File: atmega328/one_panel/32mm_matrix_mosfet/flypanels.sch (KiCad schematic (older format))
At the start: 16 parts, among them IC1 ATMEGA328-A, P1 CONN_8, P2 CONN_8, X1 CER_RESO

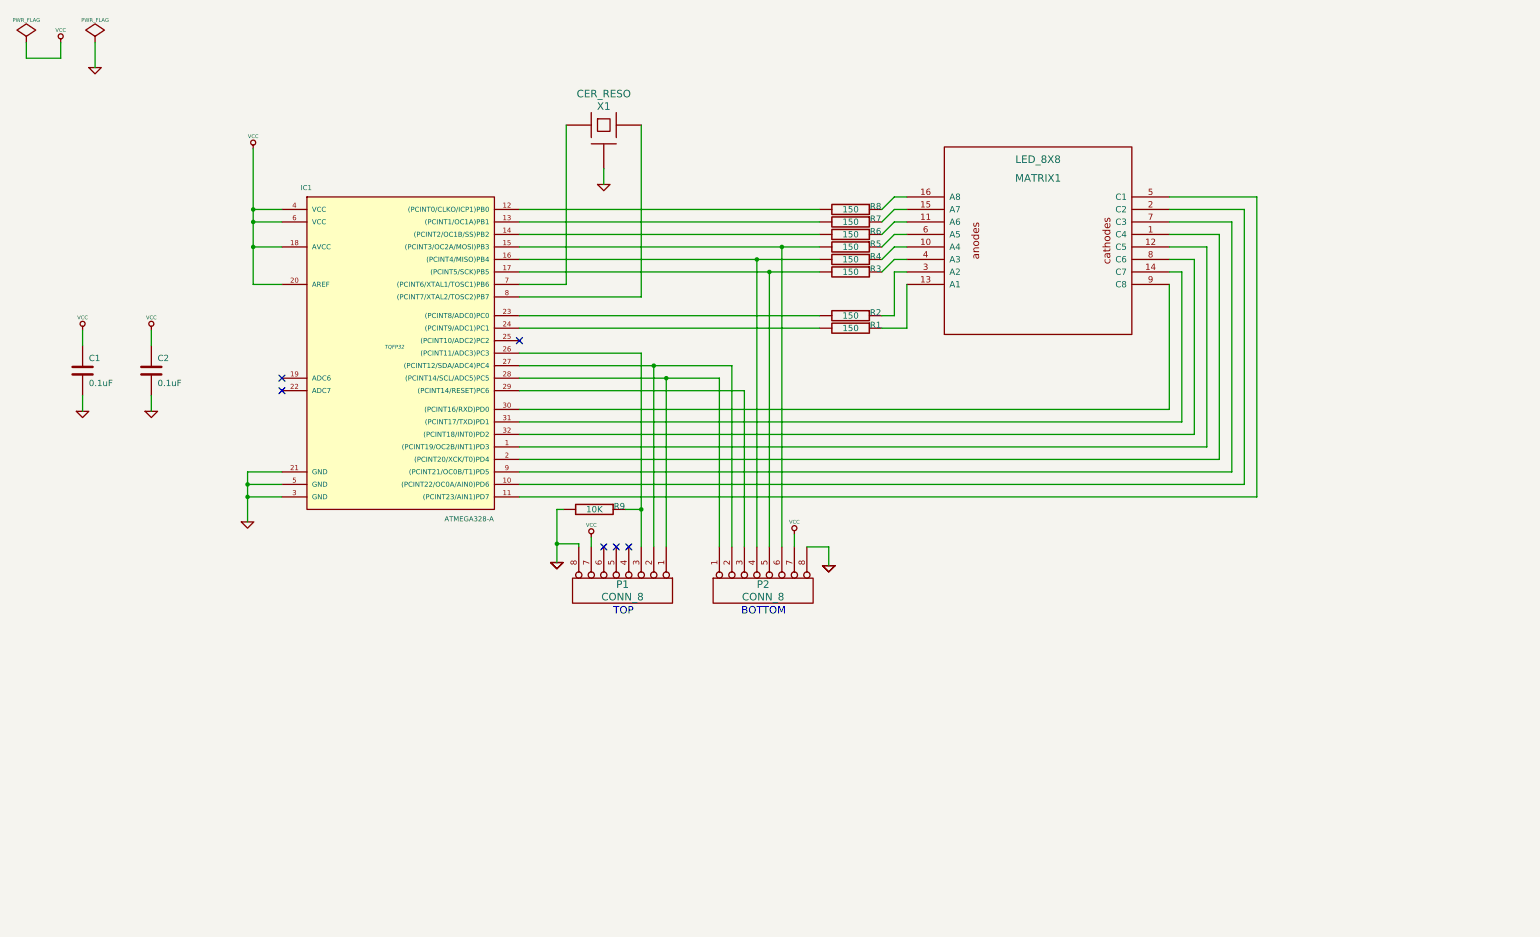
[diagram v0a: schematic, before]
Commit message: Added version of single matrix atmega328 design with mosfets.
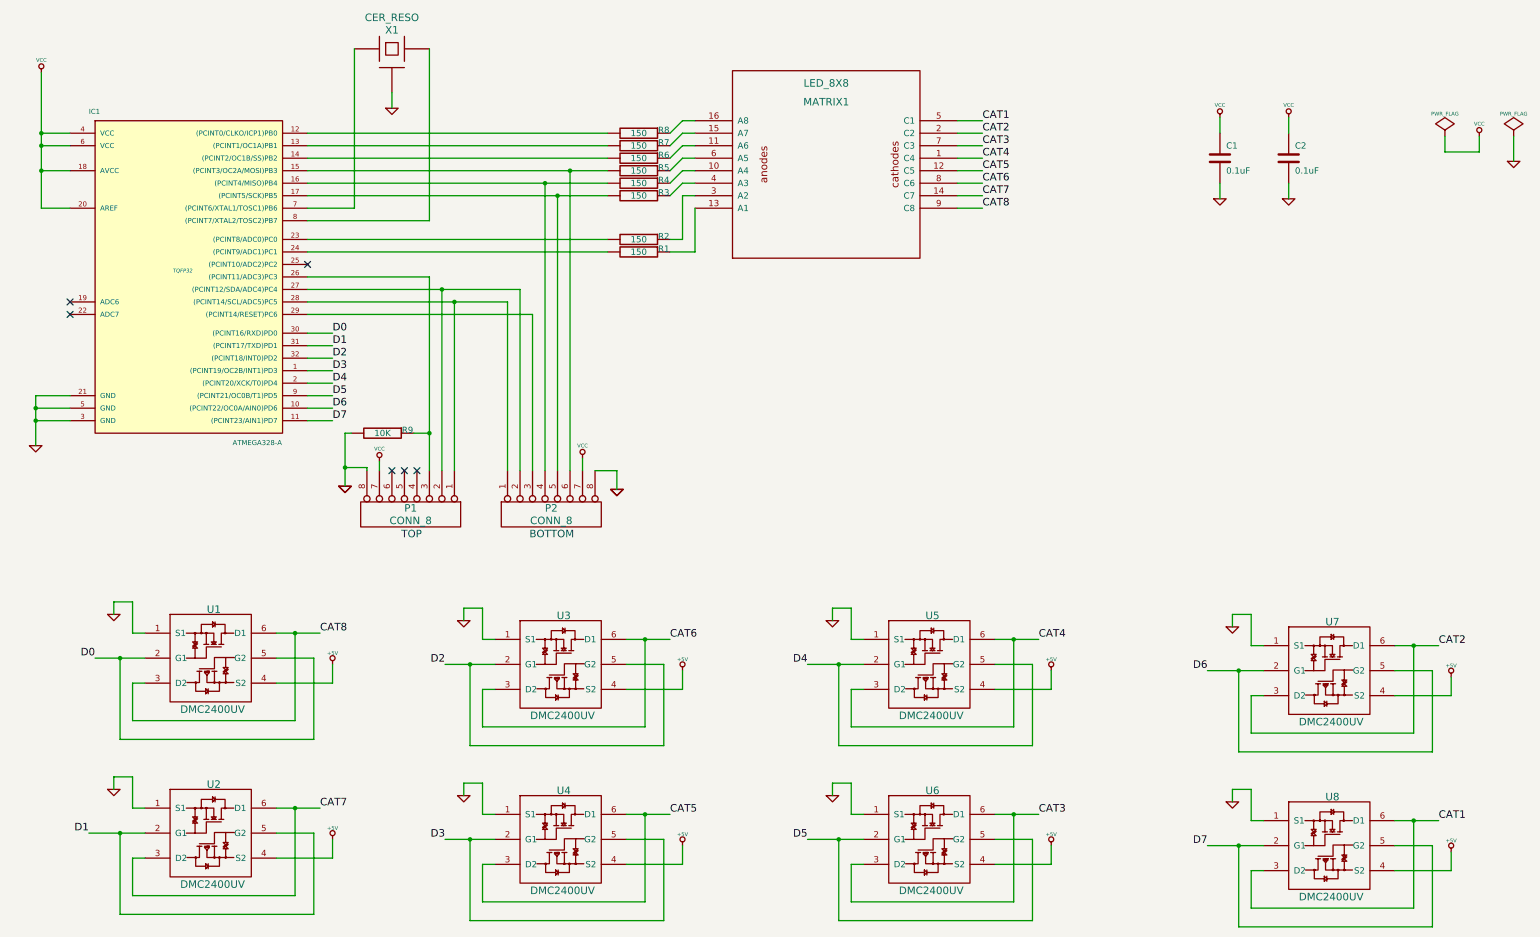
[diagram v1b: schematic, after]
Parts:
- added U1, U2, U3, U4, U5, U6, U7, U8: DMC2400UV, ~, symbol DMC2400UV
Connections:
- net GND: now also U1.1 (S1), U2.1 (S1), U3.1 (S1), U4.1 (S1), U5.1 (S1), U6.1 (S1), U7.1 (S1), U8.1 (S1)
- net CAT4: now reaches MATRIX1.1 (C4)
- net CAT4: now also U5.3 (D2), U5.6 (D1); no longer IC1.2 ((PCINT20/XCK/T0)PD4)
- net CAT5: now reaches MATRIX1.12 (C5)
- net CAT5: now also U4.3 (D2), U4.6 (D1); no longer IC1.1 ((PCINT19/OC2B/INT1)PD3)
- net CAT7: now reaches MATRIX1.14 (C7)
- net CAT7: now also U2.3 (D2), U2.6 (D1); no longer IC1.31 ((PCINT17/TXD)PD1)
- net CAT2: now reaches MATRIX1.2 (C2)
- net CAT2: now also U7.3 (D2), U7.6 (D1); no longer IC1.10 ((PCINT22/OC0A/AIN0)PD6)
- net CAT1: now reaches MATRIX1.5 (C1)
- net CAT1: now also U8.3 (D2), U8.6 (D1); no longer IC1.11 ((PCINT23/AIN1)PD7)
- net CAT3: now reaches MATRIX1.7 (C3)
- net CAT3: now also U6.3 (D2), U6.6 (D1); no longer IC1.9 ((PCINT21/OC0B/T1)PD5)
- net CAT6: now reaches MATRIX1.8 (C6)
- net CAT6: now also U3.3 (D2), U3.6 (D1); no longer IC1.32 ((PCINT18/INT0)PD2)
- net CAT8: now reaches MATRIX1.9 (C8)
- net CAT8: now also U1.3 (D2), U1.6 (D1); no longer IC1.30 ((PCINT16/RXD)PD0)
- new net +5V: U1.4 (S2), U2.4 (S2), U3.4 (S2), U4.4 (S2), U5.4 (S2), U6.4 (S2), U7.4 (S2), U8.4 (S2)
- new net D0: IC1.30 ((PCINT16/RXD)PD0), U1.2 (G1), U1.5 (G2)
- new net D1: IC1.31 ((PCINT17/TXD)PD1), U2.2 (G1), U2.5 (G2)
- new net D2: IC1.32 ((PCINT18/INT0)PD2), U3.2 (G1), U3.5 (G2)
- new net D3: IC1.1 ((PCINT19/OC2B/INT1)PD3), U4.2 (G1), U4.5 (G2)
- new net D4: IC1.2 ((PCINT20/XCK/T0)PD4), U5.2 (G1), U5.5 (G2)
- new net D5: IC1.9 ((PCINT21/OC0B/T1)PD5), U6.2 (G1), U6.5 (G2)
- new net D6: IC1.10 ((PCINT22/OC0A/AIN0)PD6), U7.2 (G1), U7.5 (G2)
- new net D7: IC1.11 ((PCINT23/AIN1)PD7), U8.2 (G1), U8.5 (G2)
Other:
- moved on the sheet: C1, C2, IC1, MATRIX1, P1, P2, R1, R2, R3, R4, R5, R6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

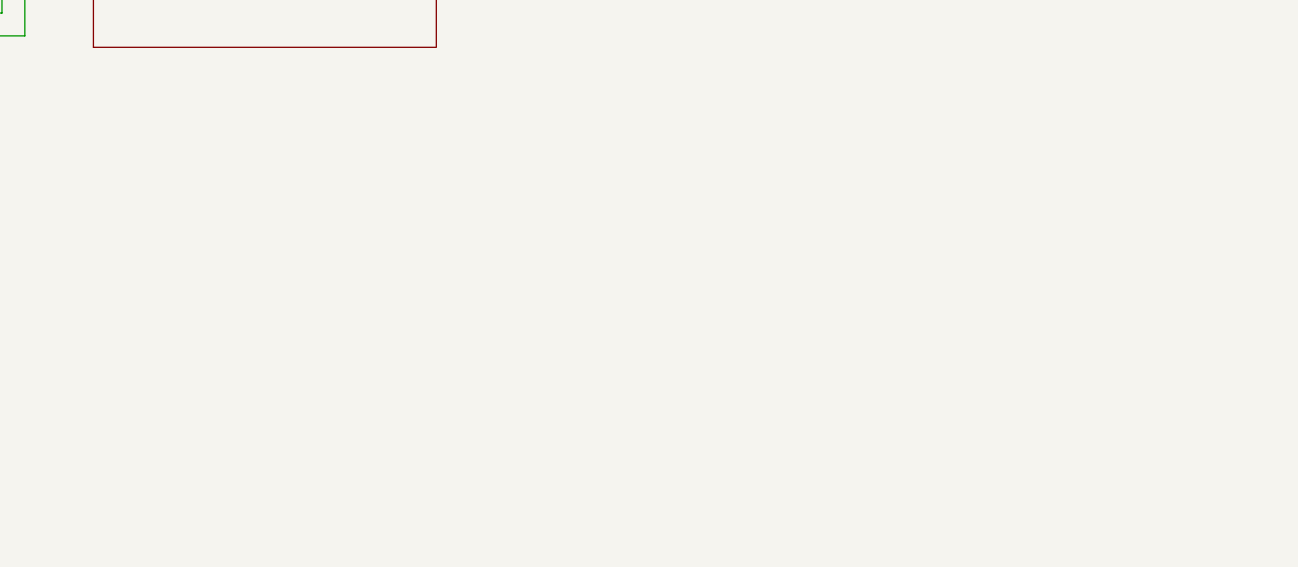
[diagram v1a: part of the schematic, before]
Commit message: Added note about error to atmega328 design.
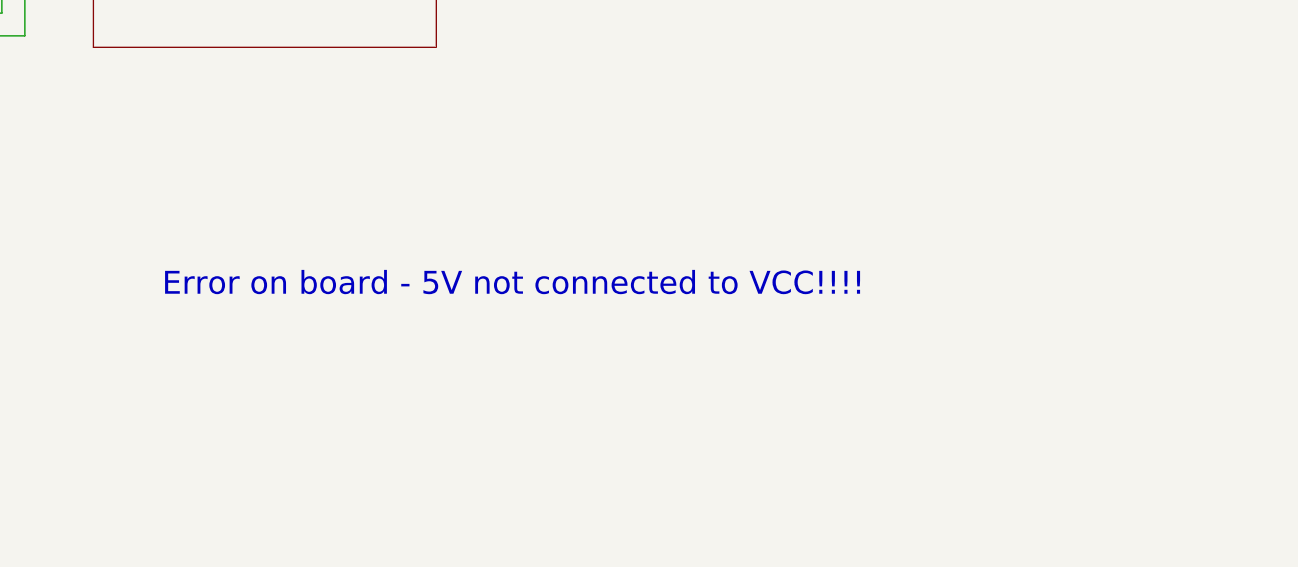
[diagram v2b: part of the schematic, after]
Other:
- note added: "Error on board - 5V not connected to VCC!!!!"
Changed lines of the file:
@@
 Sheet 1 1
 Title ""
-Date "22 may 2016"
+Date "24 jul 2016"
 Rev ""
 Comp ""
@@
 Text Label 3250 5650 0    60   ~ 0
 CAT8
+Text Notes 6850 3750 0    100  ~ 0
+Error on board - 5V not connected to VCC!!!!
 $EndSCHEMATC

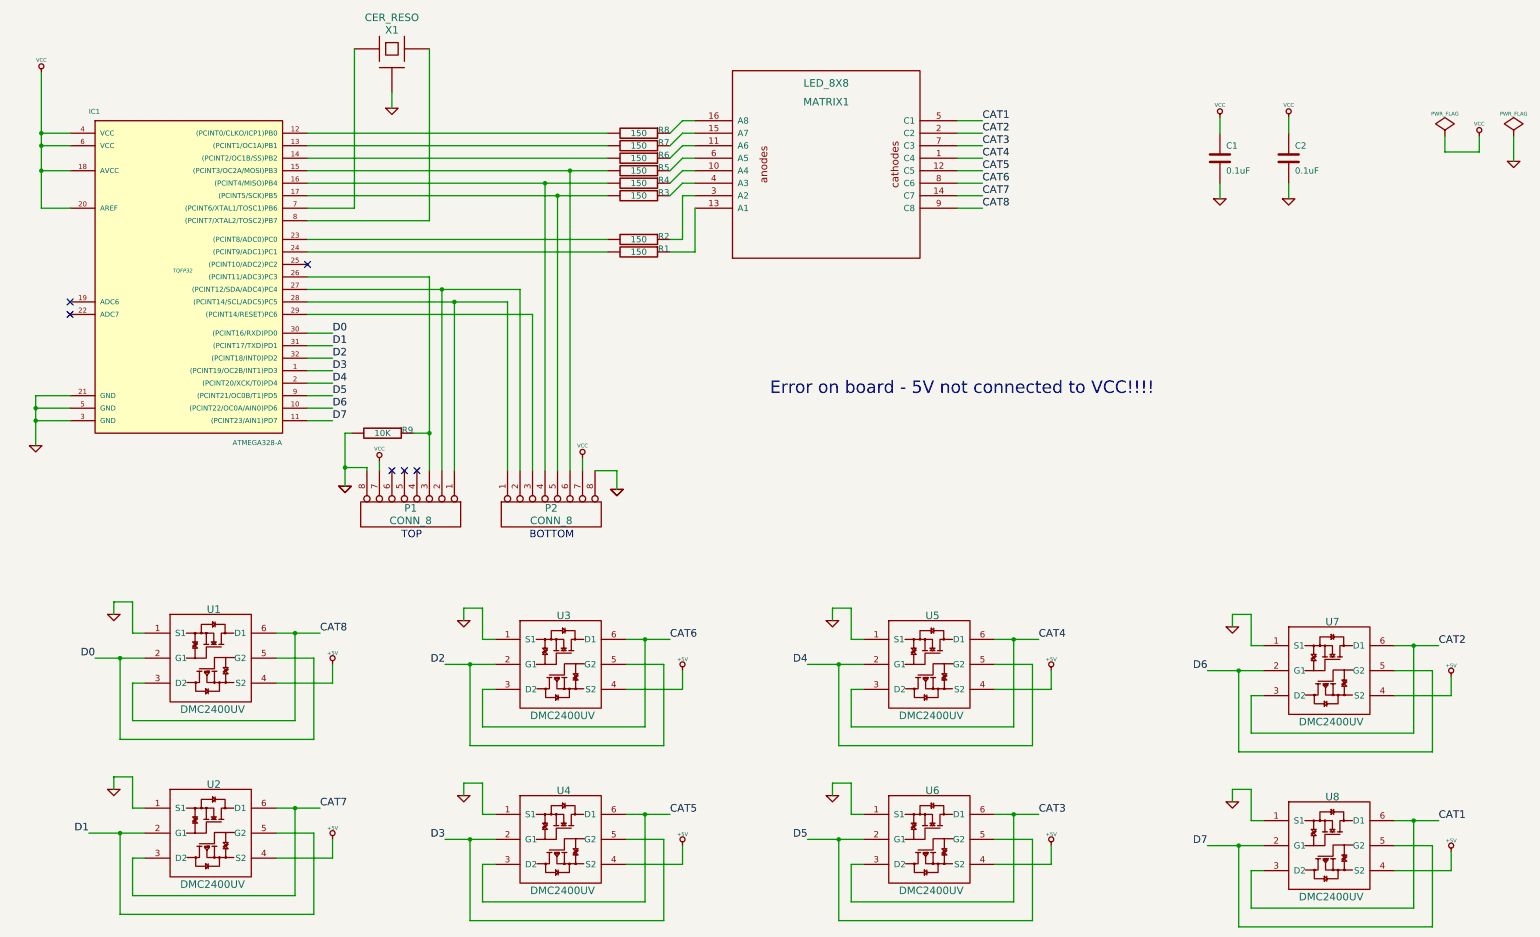
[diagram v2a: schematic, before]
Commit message: Added gerber files for 2nd revision of one matrix atmeg328.
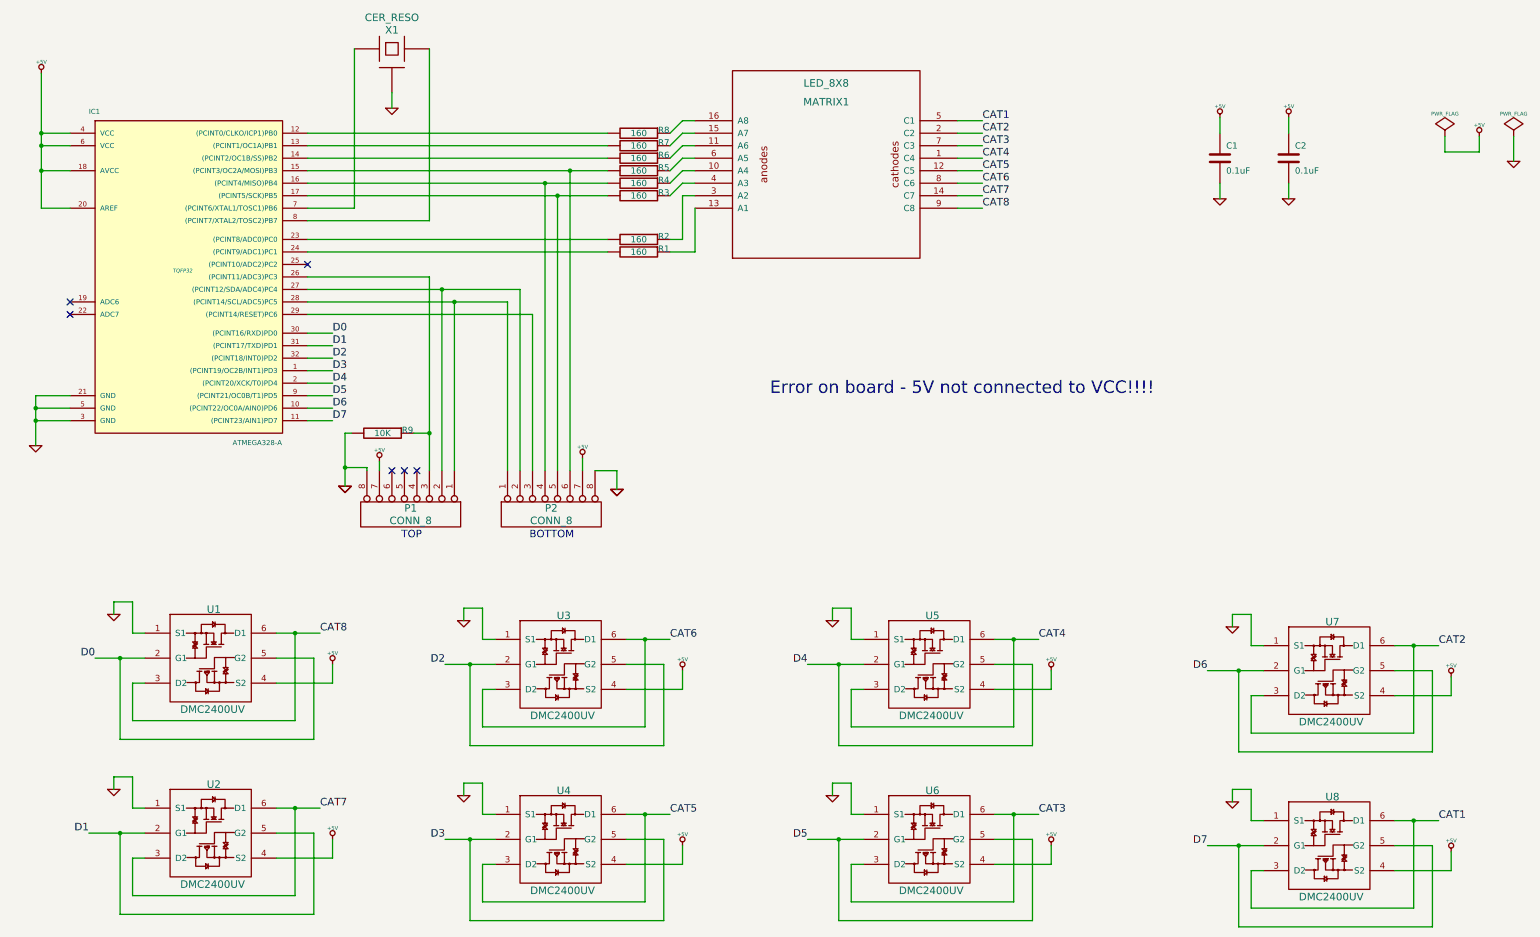
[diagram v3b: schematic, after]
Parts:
- R1, R2, R3, R4, R5, R6, R7, R8: value 150 -> 160
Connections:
- net VCC is gone; now on net +5V: C1.1, C2.1, IC1.18 (AVCC), IC1.20 (AREF), IC1.4 (VCC), IC1.6 (VCC), P1.7 (P7), P2.7 (P7)
